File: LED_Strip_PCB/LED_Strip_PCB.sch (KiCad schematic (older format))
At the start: 12 parts

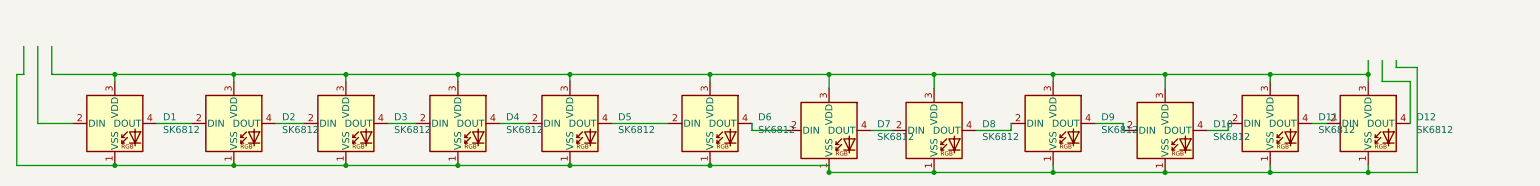
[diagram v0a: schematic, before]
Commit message: PCB now has 3 LED strips and perforation
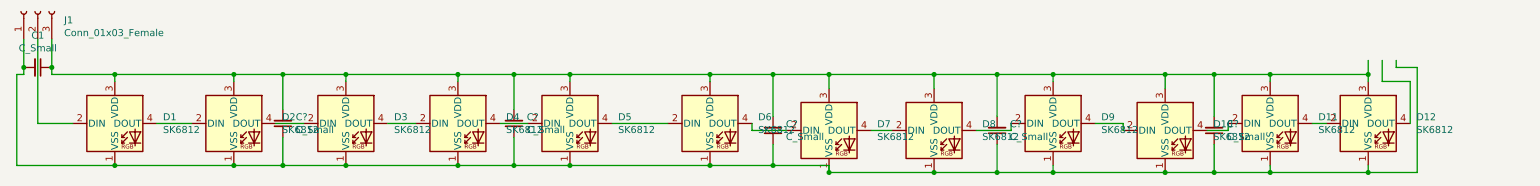
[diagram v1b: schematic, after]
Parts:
- added C1, C? (x5): C_Small, Capacitor_THT:C_Disc_D4.3mm_W1.9mm_P5.00mm, symbol Device:C_Small
- added J1: Conn_01x03_Female, Connector_PinHeader_2.54mm:PinHeader_1x03_P2.54mm_Vertical, symbol Connector:Conn_01x03_Female
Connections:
- wire segments 69 -> 91
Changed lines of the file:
@@
 $EndComp
-Wire Wire Line
-	850  2350 850  2550
 Wire Wire Line
 	1300 2550 1300 2600
 Wire Wire Line
-	650  2350 650  2550
-Wire Wire Line
 	650  2550 600  2550
 Wire Wire Line
@@
 Wire Wire Line
 	600  3200 1300 3200
-Wire Wire Line
-	750  2350 750  2900
 Wire Wire Line
 	750  2900 1000 2900
@@
 	3450 2900 3250 2900
 Wire Wire Line
-	2650 2900 2450 2900
-Wire Wire Line
 	1850 2900 1600 2900
 Wire Wire Line
@@
 	1300 2550 2150 2550
 Wire Wire Line
-	2150 2550 2950 2550
-Wire Wire Line
-	2150 3200 2950 3200
+	2150 2550 2500 2550
+Wire Wire Line
+	2150 3200 2500 3200
+Wire Wire Line
+	3750 2550 4150 2550
+Wire Wire Line
+	3750 3200 4150 3200
+Wire Wire Line
+	5550 2550 6000 2550
+Wire Wire Line
+	5550 3200 6000 3200
+Wire Wire Line
+	7150 3250 7600 3250
+Wire Wire Line
+	7150 2550 7600 2550
+Wire Wire Line
+	8800 2550 9150 2550
+Wire Wire Line
+	8800 3250 9150 3250
 Wire Wire Line
 	850  2550 1300 2550
 Wire Wire Line
-	3750 2550 4550 2550
-Wire Wire Line
-	3750 3200 4550 3200
-Wire Wire Line
-	5550 2550 6400 2550
-Wire Wire Line
-	5550 3200 6400 3200
-Wire Wire Line
-	7150 3250 8000 3250
-Wire Wire Line
-	7150 2550 8000 2550
-Wire Wire Line
-	8800 2550 9550 2550
-Wire Wire Line
-	8800 3250 9550 3250
+	650  2300 650  2500
+Wire Wire Line
+	750  2300 750  2900
+Wire Wire Line
+	850  2300 850  2500
+$Comp
+L Device:C_Small C1
+U 1 1 5E6B0113
+P 750 2500
+F 0 "C1" V 521 2500 50  0000 C CNN
+F 1 "C_Small" V 612 2500 50  0000 C CNN
+F 2 "Capacitor_THT:C_Disc_D4.3mm_W1.9mm_P5.00mm" H 750 2500 50  0001 C CNN
+F 3 "~" H 750 2500 50  0001 C CNN
+	1    750  2500
+	0    1    1    0
+$EndComp
+Connection ~ 850  2500
+Wire Wire Line
+	850  2500 850  2550
+Connection ~ 650  2500
+Wire Wire Line
+	650  2500 650  2550
+$Comp
+L Connector:Conn_01x03_Female J1
+U 1 1 5E6B7242
+P 750 2100
+F 0 "J1" V 688 1912 50  0000 R CNN
+F 1 "Conn_01x03_Female" V 597 1912 50  0000 R CNN
+F 2 "Connector_PinHeader_2.54mm:PinHeader_1x03_P2.54mm_Vertical" H 750 2100 50  0001 C CNN
+F 3 "~" H 750 2100 50  0001 C CNN
+	1    750  2100
+	0    -1   -1   0
+$EndComp
+$Comp
+L Device:C_Small C?
+U 1 1 5E6BF639
+P 2500 2900
+F 0 "C?" H 2408 2854 50  0000 R CNN
+F 1 "C_Small" H 2408 2945 50  0000 R CNN
+F 2 "Capacitor_THT:C_Disc_D4.3mm_W1.9mm_P5.00mm" H 2500 2900 50  0001 C CNN
+F 3 "~" H 2500 2900 50  0001 C CNN
+	1    2500 2900
+	-1   0    0    1
+$EndComp
+Wire Wire Line
+	2450 2900 2650 2900
+$Comp
+L Device:C_Small C?
+U 1 1 5E6C0EB8
+P 4150 2900
+F 0 "C?" H 4058 2854 50  0000 R CNN
+F 1 "C_Small" H 4058 2945 50  0000 R CNN
+F 2 "Capacitor_THT:C_Disc_D4.3mm_W1.9mm_P5.00mm" H 4150 2900 50  0001 C CNN
+F 3 "~" H 4150 2900 50  0001 C CNN
+	1    4150 2900
+	-1   0    0    1
+$EndComp
+$Comp
+L Device:C_Small C?
+U 1 1 5E6C141B
+P 6000 2950
+F 0 "C?" H 5908 2904 50  0000 R CNN
+F 1 "C_Small" H 5908 2995 50  0000 R CNN
+F 2 "Capacitor_THT:C_Disc_D4.3mm_W1.9mm_P5.00mm" H 6000 2950 50  0001 C CNN
+F 3 "~" H 6000 2950 50  0001 C CNN
+	1    6000 2950
+	-1   0    0    1
+$EndComp
+$Comp
+L Device:C_Small C?
+U 1 1 5E6C1777
+P 7600 2950
+F 0 "C?" H 7508 2904 50  0000 R CNN
+F 1 "C_Small" H 7508 2995 50  0000 R CNN
+F 2 "Capacitor_THT:C_Disc_D4.3mm_W1.9mm_P5.00mm" H 7600 2950 50  0001 C CNN
+F 3 "~" H 7600 2950 50  0001 C CNN
+	1    7600 2950
+	-1   0    0    1
+$EndComp
+$Comp
+L Device:C_Small C?
+U 1 1 5E6C1AD9
+P 9150 2950
+F 0 "C?" H 9058 2904 50  0000 R CNN
+F 1 "C_Small" H 9058 2995 50  0000 R CNN
+F 2 "Capacitor_THT:C_Disc_D4.3mm_W1.9mm_P5.00mm" H 9150 2950 50  0001 C CNN
+F 3 "~" H 9150 2950 50  0001 C CNN
+	1    9150 2950
+	-1   0    0    1
+$EndComp
+Wire Wire Line
+	9150 3050 9150 3250
+Connection ~ 9150 3250
+Wire Wire Line
+	9150 3250 9550 3250
+Wire Wire Line
+	9150 2850 9150 2550
+Connection ~ 9150 2550
+Wire Wire Line
+	9150 2550 9550 2550
+Wire Wire Line
+	7600 2850 7600 2550
+Connection ~ 7600 2550
+Wire Wire Line
+	7600 2550 8000 2550
+Wire Wire Line
+	7600 3050 7600 3250
+Connection ~ 7600 3250
+Wire Wire Line
+	7600 3250 8000 3250
+Wire Wire Line
+	6000 3050 6000 3200
+Connection ~ 6000 3200
+Wire Wire Line
+	6000 3200 6400 3200
+Wire Wire Line
+	6000 2850 6000 2550
+Connection ~ 6000 2550
+Wire Wire Line
+	6000 2550 6400 2550
+Wire Wire Line
+	4150 3000 4150 3200
+Connection ~ 4150 3200
+Wire Wire Line
+	4150 3200 4550 3200
+Wire Wire Line
+	4150 2800 4150 2550
+Connection ~ 4150 2550
+Wire Wire Line
+	4150 2550 4550 2550
+Wire Wire Line
+	2500 3000 2500 3200
+Connection ~ 2500 3200
+Wire Wire Line
+	2500 3200 2950 3200
+Wire Wire Line
+	2500 2800 2500 2550
+Connection ~ 2500 2550
+Wire Wire Line
+	2500 2550 2950 2550
 $EndSCHEMATC

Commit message: fixed silk screen over lap
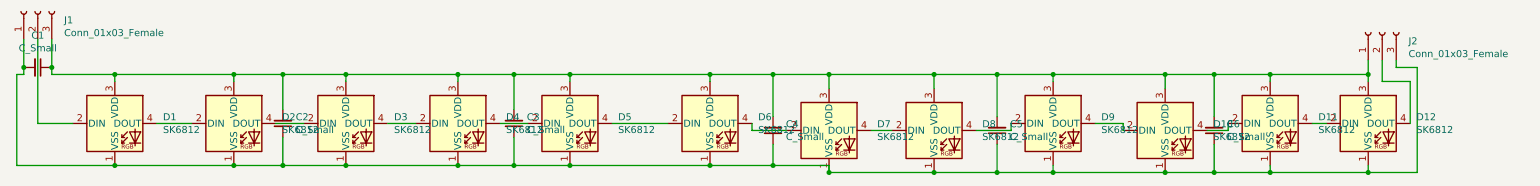
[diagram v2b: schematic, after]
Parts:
- added J2: Conn_01x03_Female, Connector_PinHeader_2.54mm:PinHeader_1x03_P2.54mm_Vertical, symbol Connector:Conn_01x03_Female
- gave numbers to parts that had none: 5
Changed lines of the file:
@@
 $EndComp
 $Comp
-L Device:C_Small C?
+L Device:C_Small C2
 U 1 1 5E6BF639
 P 2500 2900
-F 0 "C?" H 2408 2854 50  0000 R CNN
+F 0 "C2" H 2408 2854 50  0000 R CNN
 F 1 "C_Small" H 2408 2945 50  0000 R CNN
 F 2 "Capacitor_THT:C_Disc_D4.3mm_W1.9mm_P5.00mm" H 2500 2900 50  0001 C CNN
@@
 	2450 2900 2650 2900
 $Comp
-L Device:C_Small C?
+L Device:C_Small C3
 U 1 1 5E6C0EB8
 P 4150 2900
-F 0 "C?" H 4058 2854 50  0000 R CNN
+F 0 "C3" H 4058 2854 50  0000 R CNN
 F 1 "C_Small" H 4058 2945 50  0000 R CNN
 F 2 "Capacitor_THT:C_Disc_D4.3mm_W1.9mm_P5.00mm" H 4150 2900 50  0001 C CNN
@@
 $EndComp
 $Comp
-L Device:C_Small C?
+L Device:C_Small C4
 U 1 1 5E6C141B
 P 6000 2950
-F 0 "C?" H 5908 2904 50  0000 R CNN
+F 0 "C4" H 5908 2904 50  0000 R CNN
 F 1 "C_Small" H 5908 2995 50  0000 R CNN
 F 2 "Capacitor_THT:C_Disc_D4.3mm_W1.9mm_P5.00mm" H 6000 2950 50  0001 C CNN
@@
 $EndComp
 $Comp
-L Device:C_Small C?
+L Device:C_Small C5
 U 1 1 5E6C1777
 P 7600 2950
-F 0 "C?" H 7508 2904 50  0000 R CNN
+F 0 "C5" H 7508 2904 50  0000 R CNN
 F 1 "C_Small" H 7508 2995 50  0000 R CNN
 F 2 "Capacitor_THT:C_Disc_D4.3mm_W1.9mm_P5.00mm" H 7600 2950 50  0001 C CNN
@@
 $EndComp
 $Comp
-L Device:C_Small C?
+L Device:C_Small C6
 U 1 1 5E6C1AD9
 P 9150 2950
-F 0 "C?" H 9058 2904 50  0000 R CNN
+F 0 "C6" H 9058 2904 50  0000 R CNN
 F 1 "C_Small" H 9058 2995 50  0000 R CNN
 F 2 "Capacitor_THT:C_Disc_D4.3mm_W1.9mm_P5.00mm" H 9150 2950 50  0001 C CNN
@@
 Wire Wire Line
 	2500 2550 2950 2550
+$Comp
+L Connector:Conn_01x03_Female J2
+U 1 1 5E6D8263
+P 10350 2250
+F 0 "J2" V 10288 2062 50  0000 R CNN
+F 1 "Conn_01x03_Female" V 10197 2062 50  0000 R CNN
+F 2 "Connector_PinHeader_2.54mm:PinHeader_1x03_P2.54mm_Vertical" H 10350 2250 50  0001 C CNN
+F 3 "~" H 10350 2250 50  0001 C CNN
+	1    10350 2250
+	0    -1   -1   0
+$EndComp
 $EndSCHEMATC
